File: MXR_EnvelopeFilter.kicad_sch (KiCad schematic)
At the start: 55 parts, among them U1 4069UB, U2 4069UB, U3 4066BMS

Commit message: updated to use STM32
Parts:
- removed C10: 10pF, symbol MXR_EnvelopeFilter-rescue:C
- removed C12: 100pF, symbol MXR_EnvelopeFilter-rescue:CP
- removed R14: 62K, symbol MXR_EnvelopeFilter-rescue:R
- removed R16, R20, R21: 100K, symbol MXR_EnvelopeFilter-rescue:R
- removed R22, R26: 47K, symbol MXR_EnvelopeFilter-rescue:R
- removed R4: 3K3, symbol MXR_EnvelopeFilter-rescue:R
- removed SW_ON_1: SW_3PDT_on_on, symbol sw_custom:SW_3PDT_on_on
- removed U1: 4069UB, Housings_SSOP:TSSOP-14_4.4x5mm_Pitch0.65mm, symbol 4069ub:4069UB
- removed U2: 4069UB, Housings_SOIC:SOIC-14_3.9x8.7mm_Pitch1.27mm, symbol 4069ub:4069UB
- removed U3: 4066BMS, symbol 4066bms:4066BMS
- added C11, C16, C5: 10uF, Capacitor_SMD:C_0805_2012Metric_Pad1.18x1.45mm_HandSolder, symbol Device:C
- added C13, C14: 100nF, Capacitor_SMD:C_0805_2012Metric_Pad1.18x1.45mm_HandSolder, symbol Device:C
- added C2, C9: 1uF, Capacitor_SMD:C_0805_2012Metric_Pad1.18x1.45mm_HandSolder, symbol Device:C
- added C?: 100p, symbol Device:C
- added D5: 1N4148, symbol Device:D
- added DIR1: SW_SPDT, symbol Switch:SW_SPDT
- added J?: Conn_02x05_Odd_Even, symbol Connector_Generic:Conn_02x05_Odd_Even
- added Q1: Q_NMOS_GSD, symbol Device:Q_NMOS_GSD
- added R? (x2): 10M, symbol Device:R
- added R?: 47k, symbol MXR_EnvelopeFilter-rescue:R
- added R? (x3): 10K, symbol Device:R
- added RL1: HFD4/3-S1, elay_THT:Relay_DPDT_Omron_G2RL, symbol Relay:G2RL-2-ASI-DC5
- added RV?: R_Potentiometer_Trim, symbol Device:R_Potentiometer_Trim
- added SW1: SW_SPST, symbol Switch:SW_SPST
- added U4, U5: SE8233X2, Package_TO_SOT_SMD:SOT-23, symbol Regulator_Linear:MCP1700-3302E_SOT23
- added U6: STM32L011D4Px, Package_SO:TSSOP-14_4.4x5mm_P0.65mm, symbol MCU_ST_STM32L0:STM32L011D4Px
- added U? (x14): 4069, symbol 4xxx:4069
- added U? (x5): 4066, symbol 4xxx:4066
- gave numbers to parts that had none: 8
- renumbered C3 to C1, C6 to C10, C1 to C12, C2 to C15, C5 to C4, C7 to C6, C9 to C7, D4 to D1, D3 to D2, D1 to D3, D2 to D4, R27 to R1, R4 to R10, R18 to R11, R11 to R12, R12 to R15, R19 to R17, R17 to R18, R8 to R2, R24 to R20, R15 to R21, R10 to R22, R25 to R23, R3 to R24, R9 to R25, R23 to R26, R1 to R27, R7 to R3, R6 to R4, R13 to R8, R5 to R9
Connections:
- net +9V: now also C7.1, D3.1 (K), R18.1, C2.2, C9.2, RV?.3, U4.3 (VI), U5.3 (VI), U?.14 (VDD), U?.14 (VDD), U?.14 (VDD); no longer R10.2
- net GND: now also D2.1 (K), C11.1, C13.2, C14.2, C16.1, C2.1, C5.1, C9.1, D5.2 (A), J?.3 (Pin_3), J?.5 (Pin_5), J?.9 (Pin_9), RL1.1, RV?.1, SW1.1 (A), U4.1 (GND), U5.1 (GND), U6.1 (PB9), U6.9 (VSS), U?.7 (VSS), U?.7 (VSS), U?.7 (VSS)
- net at R2.2, R3.2: now also RL1.5; no longer C1.1
- net at C1.2, R1.1: now also J1.T
- net at R15.2, R3.1, R8.2: now also U?.1
- net at R11.2, R8.1: now also U?.2
- net at R11.1: now also U?.2
- net at C10.2, R23.1: now also U?.5
- net at R23.2: now also U?.4
- net at C10.1, R15.1: now also RL1.4, U?.6; no longer C15.2
- net at R27.1: now also J2.T
- net at R2.1, R4.2: now also U?.1
- net at R9.1: now also THRESH1.2; no longer THRESH1.1
- net at R4.1, R9.2: now also U?.2
- net at R12.2, THRESH1.3: now also U?.3; no longer THRESH1.2
- net at C4.2, R12.1: now also U?.4
- net at R20.1, R21.2: now also U?.5
- net at R21.1, R22.1: now also U?.6
- net at R24.1, R25.2: now also U?.9
- net at ATTACK1.2, C12.2, R24.2: now also ATTACK1.3
- net at C12.1, R25.1, R26.2: now also U?.8
- net at C6.2, R17.2: now also U?.1, U?.3
- net at C6.1, R17.1: now also U?.3, U?.4
- net at R26.1: now also R?.1, U?.11, U?.12
- net at TP4.1: now also U?.9
- net at TP6.1: now also U?.8
- net at TP5.1: now also U?.6
- net at TP1.1: now also U?.10
- net at TP3.1: now also U?.11
- net at TP2.1: now also U?.12
- new net: C1.1, R?.1
- new net: C15.2, RL1.3
- new net: R10.2, U6.11 (PA9)
- new net: R?.1, R?.2, U?.9
- new net: R?.2, RL1.6, U?.8
- new net: C5.2, Q1.3 (D), U4.2 (VO)
- new net: DIR1.3 (C), U?.12, U?.13, U?.5
- new net: R?.1, R?.1, R?.2, U?.13
- new net: Q1.1 (G), U6.8 (PA7)
- new net: D5.1 (K), Q1.2 (S), RL1.8
- new net: RL1.2, RL1.7
- new net: C?.2, R?.2, U?.11
- new net: DIR1.1 (A), U?.13
- new net: DIR1.2 (B), U?.10
- new net: R?.2, RV?.2
- new net: C?.1, R?.2, U?.10
- new net +3V3: C11.2, C13.1, C16.2, J?.1 (Pin_1), U5.2 (VO), U6.10 (VDD)
- new net SWCLK: J?.2 (Pin_2), J?.4 (Pin_4), U6.13 (PA13), U6.14 (PA14)
- new net TIM2_CH1: R?.1, U6.5 (PA0)
- new net TIM2_CH2: U6.6 (PA1)
- new net TIM2_CH3: U6.12 (PA10)
- new net nRESET: C14.1, J?.10 (Pin_10), SW1.2 (B), U6.4 (NRST)
- no-connect marks 7 -> 9
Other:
- note added: "Always boot from flash"
- note added: "BOOT0"
- note removed: "| --- CMOS Square wave Oscillator (U1A + U1B) --- | with smoothing Integrator filter (U2C)"
- note removed: "| --------------------- 2 OpAmp Peak Detector------------------ | THRESH1 adjusts sensitivity of U1D Peak Detector (with D1, D2, C9), Unity Gain Inverter U1F provides phase correction"
- moved on the sheet: ATTACK1, C1, C10, C12, C15, C4, C6, C7, D1, D2, D3, D4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

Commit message: updated
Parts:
- removed ATTACK1: 500K_B, symbol MXR_EnvelopeFilter-rescue:POT
- removed J1, J2: AudioJack2_Switch, symbol Connector:AudioJack2_Switch
- removed J_P1: BARREL_JACK, symbol MXR_EnvelopeFilter-rescue:BARREL_JACK
- removed THRESH1: 100K_B, symbol MXR_EnvelopeFilter-rescue:POT
- added J1, J4, J5: Conn_01x02, symbol Connector_Generic:Conn_01x02
- added J3: Conn_01x02, Connector_PinHeader_2.54mm:PinHeader_1x02_P2.54mm_Vertical, symbol Connector_Generic:Conn_01x02
- added JP1: Jumper_2_Bridged, symbol Jumper:Jumper_2_Bridged
- added J_ATTACK1, J_THRESH1: Conn_01x03, symbol Connector_Generic:Conn_01x03
- added TP10, TP11, TP12, TP13, TP14, TP15, TP16, TP17, TP18, TP19, TP20, TP7, TP8, TP9: TestPoint, TestPoint:TestPoint_Pad_D1.0mm, symbol Connector:TestPoint
- gave numbers to parts that had none: 12
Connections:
- net +3V3: now also TP11.1; no longer C11.2, C13.1, C16.2, U5.2 (VO), U6.10 (VDD)
- net GND: now also J1.1 (Pin_1), J3.1 (Pin_1), J4.1 (Pin_1), J5.1 (Pin_1), JP1.2 (B), TP12.1; no longer U6.1 (PB9)
- net SWCLK: now also TP16.1; no longer J2.2 (Pin_2), U6.13 (PA13)
- net nRESET: now also TP10.1
- net at C1.2, R1.1: now also J1.2 (Pin_2)
- net at R27.1: now also J3.2 (Pin_2)
- net at R9.1: now also J_THRESH1.2 (Pin_2)
- net at R12.2, U2.3: now also J_THRESH1.1 (Pin_1)
- net at R22.2: now also J_ATTACK1.3 (Pin_3)
- net at C12.2, R24.2: now also J_ATTACK1.1 (Pin_1), J_ATTACK1.2 (Pin_2)
- net at D1.2 (A): now also J4.2 (Pin_2)
- net LED: now reaches R10.2, U6.11 (PA9)
- net LED: now also TP20.1
- net RELAY: now reaches Q1.1 (G), U6.8 (PA7)
- net RELAY: now also TP19.1
- net FOOTSW: now reaches U6.2 (PC14)
- net FOOTSW: now also J5.2 (Pin_2), TP7.1
- net at U6.3 (PC15): now also TP8.1
- net at U6.7 (PA4): now also TP14.1
- net TIM2_CH1 renamed LFO
- net LFO: now also TP18.1
- net TIM2_CH2: no longer names the net of U6.6 (PA1)
- net TIM2_CH2: now also TP13.1
- net TIM2_CH3: no longer names the net of U6.12 (PA10)
- net TIM2_CH3: now also TP15.1
- new net: JP1.1 (A), TP9.1, U6.1 (PB9)
- new net: C11.2, C13.1, C16.2, U5.2 (VO), U6.10 (VDD)
- new net SWDIO: J2.2 (Pin_2), TP17.1, U6.13 (PA13)
- no-connect marks 9 -> 4
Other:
- note added: "100K Linear"
- note added: "500K Linear"
- note removed: "| ----------------------- 3 Stage State Variant Filter (SVF) ---------------------------|"
- moved on the sheet: C1, C10, C11, C12, C13, C14, C15, C16, C2, C3, C4, C5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

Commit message: Modified schematic
- Moved MCU to separate sheet
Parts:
- removed C11, C16: 10uF, Capacitor_SMD:C_0805_2012Metric_Pad1.18x1.45mm_HandSolder, symbol Device:C
- removed C13, C14: 100nF, Capacitor_SMD:C_0805_2012Metric_Pad1.18x1.45mm_HandSolder, symbol Device:C
- removed C9: 1uF, Capacitor_SMD:C_0805_2012Metric_Pad1.18x1.45mm_HandSolder, symbol Device:C
- removed J2: Conn_02x05_Odd_Even, symbol Connector_Generic:Conn_02x05_Odd_Even
- removed JP1: Jumper_2_Bridged, symbol Jumper:Jumper_2_Bridged
- removed SW1: SW_SPST, symbol Switch:SW_SPST
- removed TP10, TP11, TP12, TP13, TP14, TP15, TP16, TP17, TP18, TP19, TP20, TP7, TP8, TP9: TestPoint, TestPoint:TestPoint_Pad_D1.0mm, symbol Connector:TestPoint
- removed U5: SE8233X2, Package_TO_SOT_SMD:SOT-23, symbol Regulator_Linear:MCP1700-3302E_SOT23
- removed U6: STM32L011D4Px, Package_SO:TSSOP-14_4.4x5mm_P0.65mm, symbol MCU_ST_STM32L0:STM32L011D4Px
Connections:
- net +3V3: now also C5.2, Q1.3 (D), U1.14 (VDD), U4.2 (VO)
- net +9V: no longer U1.14 (VDD)
- net at C1.2, R1.1: now also RL1.5; no longer J1.2 (Pin_2)
- net at R2.2, R3.2: now also R6.2, U2.8; no longer RL1.5
- net at C10.1, R15.1, U3.6: now also C15.2; no longer RL1.4
- net at RL1.3: now also J3.2 (Pin_2); no longer C15.2
- net at R27.1: now also RL1.4; no longer J3.2 (Pin_2)
- net FOOTSW renamed PedalController/FOOTSW
- net LED renamed PedalController/FX_LED
- net LFO renamed PedalController/FX_CLOCK
- new net: J1.2 (Pin_2), RL1.6
- no-connect marks 4 -> 1
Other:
- added sheet PedalController (PedalController.kicad_sch)
- note removed: "Always boot from flash"
- note removed: "BOOT0"
- moved on the sheet: C1, C12, C15, C2, C3, C5, D1, D2, J3, J4, J5, R1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

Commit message: Added bitcrusher effect path
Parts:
- removed C3: 100p, symbol Device:C
- removed R14: 10K, symbol Device:R
- removed R16: 47k, symbol MXR_EnvelopeFilter-rescue:R
- removed RV1: R_Potentiometer_Trim, symbol Device:R_Potentiometer_Trim
- removed TP1, TP2, TP3, TP4, TP5, TP6: TestPoint, TestPoint:TestPoint_Pad_D1.0mm, symbol Connector:TestPoint
- added C16: 10nF, symbol Device:C
- added D6, D7: D, symbol Device:D
- added J6, J7: Conn_01x03, symbol Connector_Generic:Conn_01x03
- added J8: Conn_01x02, symbol Connector_Generic:Conn_01x02
- added SPDT2, SPDT3: SW_SPDT, symbol Switch:SW_SPDT
- renumbered DIR1 to SPDT1
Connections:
- net +3V3: now also J6.1 (Pin_1), J7.1 (Pin_1), SPDT3.3 (C)
- net GND: now also C16.2, J6.3 (Pin_3), J7.3 (Pin_3), J8.1 (Pin_1), SPDT3.1 (A)
- net at C10.1, R15.1, U3.6: now also U1.9; no longer C15.2
- net at R7.1, U3.12: now also C15.2; no longer R26.1, U2.11
- net at R7.2, U3.13: now also U1.8, C16.1; no longer R13.1
- net at U1.6: now also R13.2
- net at U1.11: now also D7.1 (K)
- net at U3.11: now also SPDT2.1 (A)
- net at U2.10: now also D6.2 (A), D7.2 (A); no longer SPDT1.2 (B)
- net at U1.12: now also SPDT3.2 (B)
- net at U3.10: now also R13.1, SPDT2.3 (C)
- net PedalController/FX_PWM_CLK2: now reaches U1.10
- net PedalController/FX_PWM_CLK2: now also SPDT2.2 (B)
- new net: R26.1, U2.11
- new net PedalController/FX_PWM_CLK1: D6.1 (K), SPDT1.2 (B)
- new net PedalController/MODESW: J8.2 (Pin_2)
- new net PedalController/POT1: J6.2 (Pin_2)
- new net PedalController/POT2: J7.2 (Pin_2)
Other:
- sheet PedalController ports: added FX_PWM_CLK1, FX_PWM_CLK2, MODESW, POT1, POT2; removed FX_CLOCK
- note added: "BITCRUSH ENV MIX"
- note added: "BITCRUSH SWEEP DIRECTION"
- note added: "Bitcrusher/SampleHold"
- note added: "ENV SWEEP DIRECTION"
- note added: "Input Buffer"
- note added: "Peak Detector"
- note added: "State Variable Filter"
- moved on the sheet: C12, C2, C4, C5, C7, D1, D2, D3, D4, J4, J5, J_ATTACK1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

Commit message: Fixed some issues, generated PDF
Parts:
- removed D2: LED, symbol MXR_EnvelopeFilter-rescue:LED
- removed D6, D7: D, symbol Device:D
- removed SPDT1, SPDT2, SPDT3: SW_SPDT, symbol Switch:SW_SPDT
- added J_LED1, J_SPST1: Conn_01x02, symbol Connector_Generic:Conn_01x02
- added J_SPDT1, J_SPDT3: Conn_01x03, symbol Connector_Generic:Conn_01x03
- renumbered J5 to J_FOOTSW1, J1 to J_INPUT1, J8 to J_MODESW1, J3 to J_OUTPUT1, J6 to J_POT1, J7 to J_POT2
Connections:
- net GND: now also J_LED1.1 (Pin_1)
- net PedalController/FX_PWM_CLK1: now also U2.10, J_SPDT1.1 (Pin_1)
- net PedalController/FX_PWM_CLK2: now also J_SPDT3.1 (Pin_1), J_SPST1.2 (Pin_2); no longer U1.10
- net at R2.2, R3.2: now also U1.11; no longer R6.2, U2.8
- net at R26.1, U2.11: now also U3.11
- net at R10.1: now also J_LED1.2 (Pin_2)
- net PRE_CRUSH: now reaches U1.12
- net PRE_CRUSH: now also J_SPDT3.3 (Pin_3)
- net at U1.13, U1.5, U2.12: now also J_SPDT1.2 (Pin_2)
- net at U3.10: now also J_SPST1.1 (Pin_1); no longer R13.1
- net at U2.13: now also J_SPDT1.3 (Pin_3)
- new net: R6.2, U1.10, U2.8
- new net POST_CRUSH: J_SPDT3.2 (Pin_2), R13.1
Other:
- note added: "BITCRUSH PRE_POST"
- note removed: "BITCRUSH SWEEP DIRECTION"
- moved on the sheet: C1, C10, C6, J_MODESW1, J_POT1, J_POT2, R1, R11, R15, R17, R23, R3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

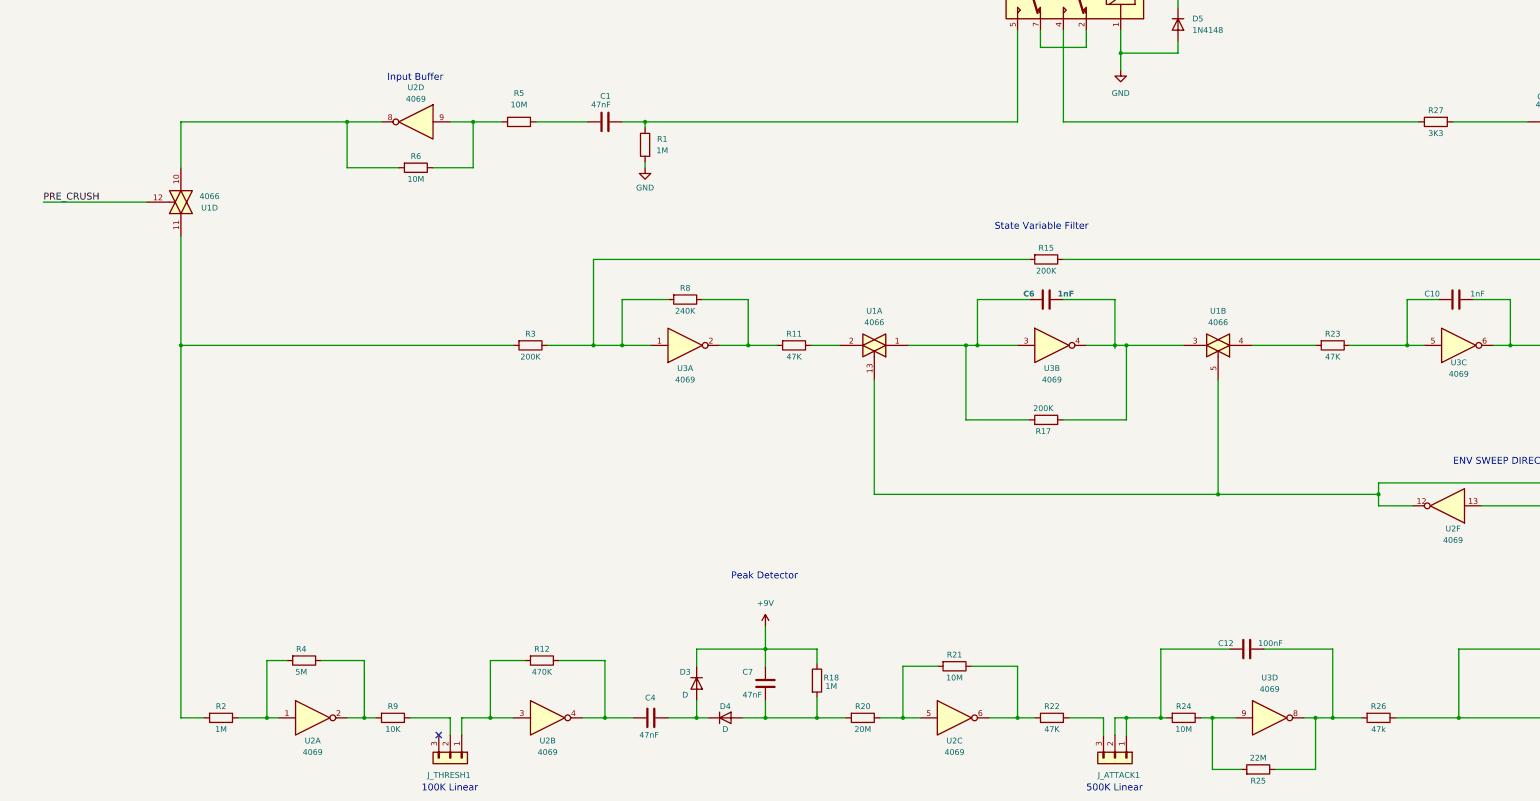
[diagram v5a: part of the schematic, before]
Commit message: Added missng cap, added more testpoints
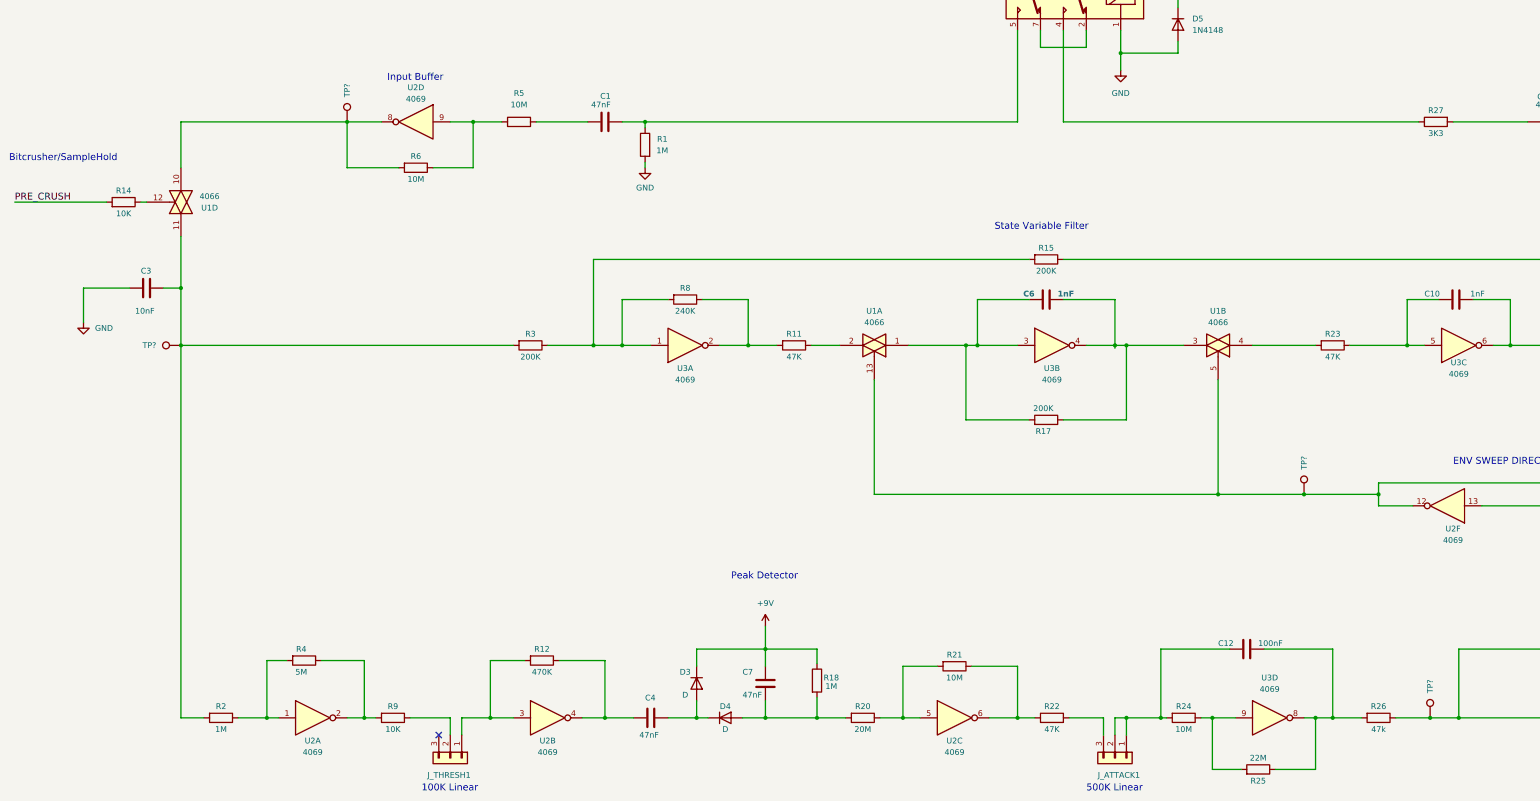
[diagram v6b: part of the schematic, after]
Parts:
- added C3: 10nF, symbol Device:C
- added R14: 10K, symbol Device:R
- added TP? (x4): TestPoint, TestPoint:TestPoint_Pad_D1.0mm, symbol Connector:TestPoint
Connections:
- net GND: now also C3.2
- net PRE_CRUSH: now also R14.2; no longer U1.12
- net at R2.2, R3.2, U1.11: now also C3.1, TP?.1
- net at R26.1, U2.11, U3.11: now also TP?.1
- net at R6.2, U1.10, U2.8: now also TP?.1
- net at J_SPDT1.2 (Pin_2), U1.13, U1.5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: now also TP?.1
- new net: R14.1, U1.12
